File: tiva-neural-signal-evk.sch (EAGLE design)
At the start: 68 parts, among them IC1 TM4C123G, IC2 TLV70233, IC3 INA2332, IC4 OPA2320, IC5 OPA2320, IC6 INA2332, IC7 OPA2320, IC8 OPA2320, X1 USB, X2 MICROSD, Y1 16MHz, Y2 32.768kHz

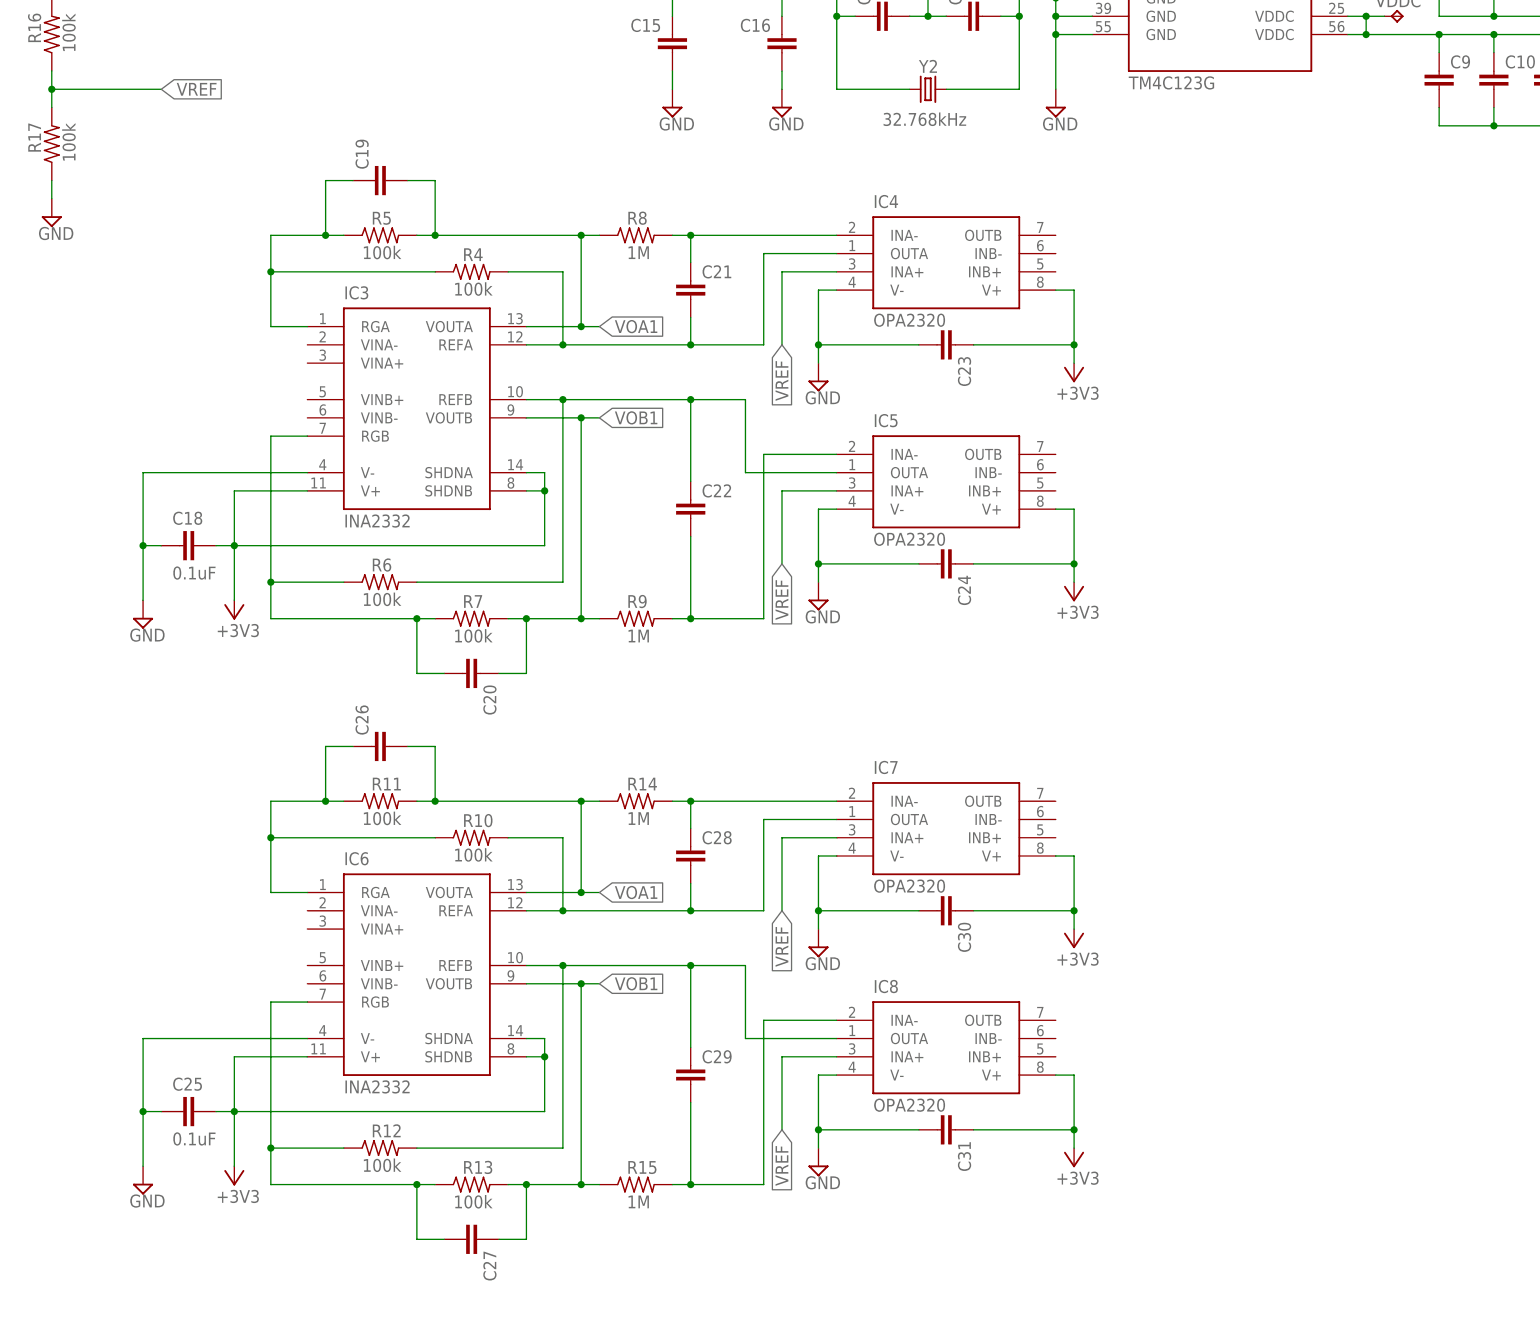
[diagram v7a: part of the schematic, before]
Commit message: completed amplifier stage design
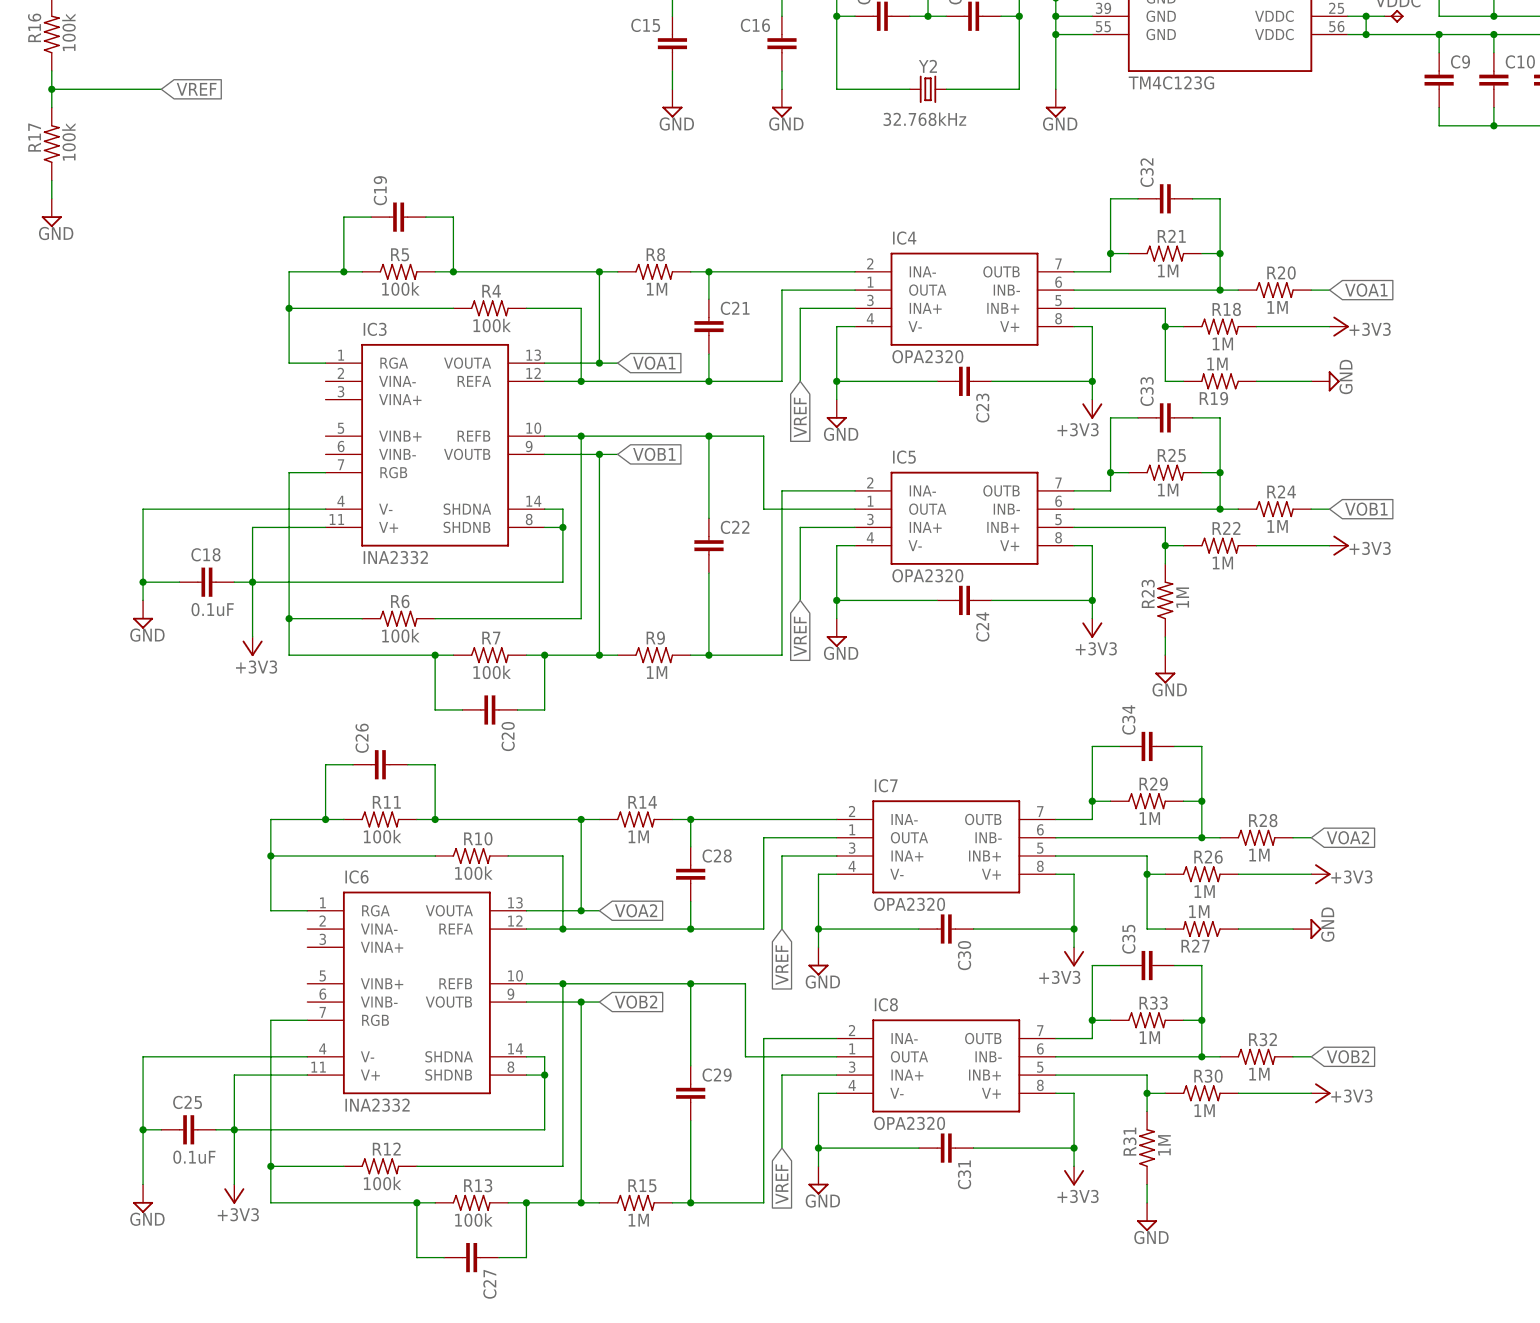
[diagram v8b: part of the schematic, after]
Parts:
- added C32, C33, C34, C35: (no value), rcl:C-EUC0603
- added R18, R19, R20, R21, R22, R23, R24, R25, R26, R27, R28, R29, R30, R31, R32, R33: 1M, rcl:R-US_R0603
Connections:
- new net N$19: IC4.INB+, R18.1, R19.2
- new net N$20: C32.2, IC4.INB-, R20.1, R21.2
- new net N$21: C32.1, IC4.OUTB, R21.1
- new net N$22: IC7.INB+, R26.1, R27.2
- new net N$23: IC5.INB+, R22.1, R23.2
- new net N$24: C33.2, IC5.INB-, R24.1, R25.2
- new net N$25: C33.1, IC5.OUTB, R25.1
- new net N$26: C34.2, IC7.INB-, R28.1, R29.2
- new net N$27: C34.1, IC7.OUTB, R29.1
- new net N$28: IC8.INB+, R30.1, R31.2
- new net N$29: C35.2, IC8.INB-, R32.1, R33.2
- new net N$30: C35.1, IC8.OUTB, R33.1
- new net VOA2: C26.2, IC6.VOUTA, R11.2, R14.1, R28.2
- new net VOB2: C27.1, IC6.VOUTB, R13.2, R15.1, R32.2
- net +3V3: now also R18.2, R22.2, R26.2, R30.2
- net GND: now also R19.1, R23.1, R27.1, R31.1
- net VOA1: now also R20.2; no longer C26.2, IC6.VOUTA, R11.2, R14.1
- net VOB1: now also R24.2; no longer C27.1, IC6.VOUTB, R13.2, R15.1
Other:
- moved on the sheet: C18, C19, C20, C21, C22, C23, C24, C25, C26, C27, C28, C29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
